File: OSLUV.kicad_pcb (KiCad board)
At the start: 4 copper layers, 110 x 85 mm, 244 parts, among them IC1 NCP12510ASN65T1G, IC2 SFH6156-3, IC3 INA210, IC4 AP63300WU-7, IC5 AP63300WU-7, IC6 STM32G071KBT6, IC7 TLV9001IDBVR, IC8 1ED44175N01BXTSA1, IC9 LP2985-33DBVR, J1 B08B-XASK-1-A_LF__SN_, J3 BM02B-SRSS-TB_LF__SN_, J4 BM02B-SRSS-TB_LF__SN_, J5 640445-2, J6 640445-2, J7 B5P-VH, Q1 STD3NK80ZT4, Q2 BC847, Q3 BSS138, Q4 BC807, Q6 BC847, T4 IMBG120R181M2HXTMA1, U1 OPA2356AIDGKR, U2 AZ431LANTR, U3 LM2901, U4 Prog

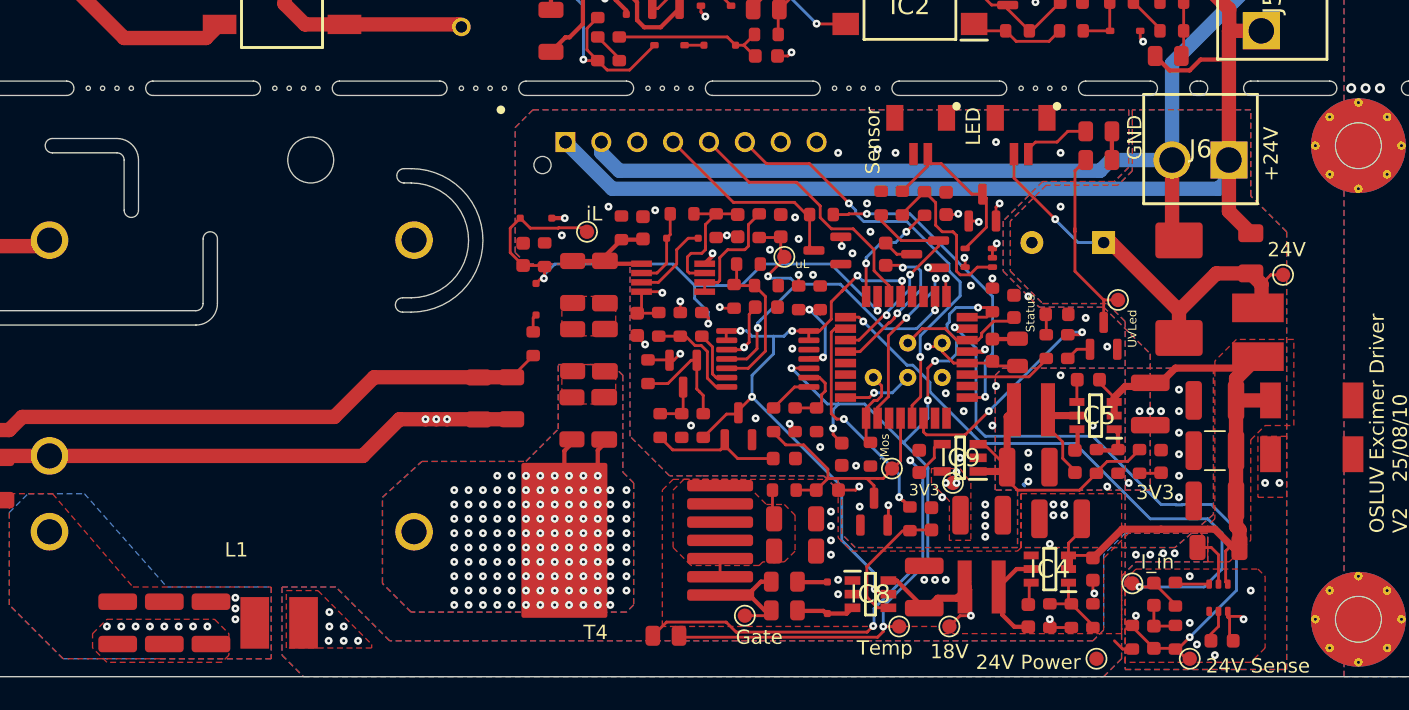
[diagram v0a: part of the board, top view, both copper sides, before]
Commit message: prototyp V2 with bug fixes
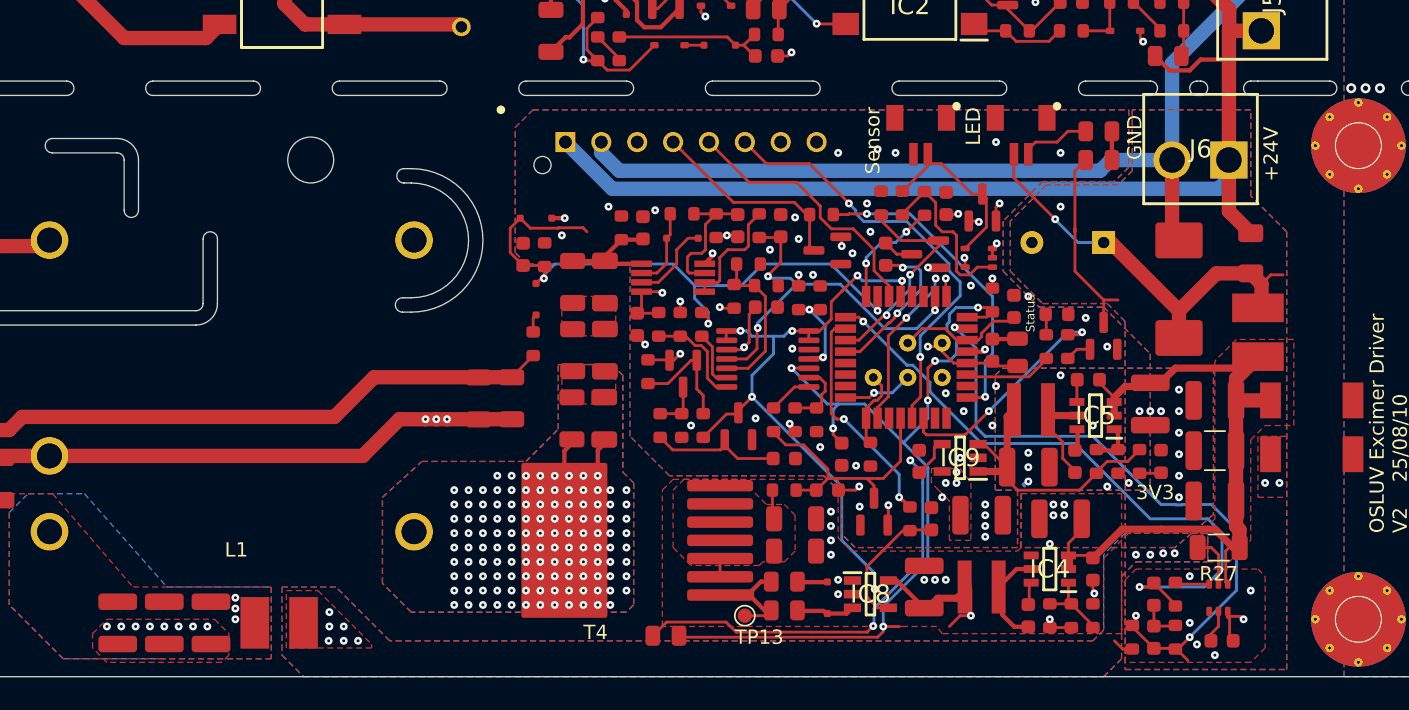
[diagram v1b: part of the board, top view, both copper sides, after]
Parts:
- removed 18V: 18V, TestPoint:TestPoint_Pad_D1.0mm
- removed 24V: 24V, TestPoint:TestPoint_Pad_D1.0mm
- removed 24V Power: VDC_Power, TestPoint:TestPoint_Pad_D1.0mm
- removed 24V Sense: 24V_Sense, TestPoint:TestPoint_Pad_D1.0mm
- removed 3V3: 3V3, TestPoint:TestPoint_Pad_D1.0mm
- removed I_in: Isense, TestPoint:TestPoint_Pad_D1.0mm
- removed REF** (x24): Loch_0,3mm, Hansmann:Loch_0,3mm
- removed Temp: Temp, TestPoint:TestPoint_Pad_D1.0mm
- removed UVLed: UV_LED, TestPoint:TestPoint_Pad_D1.0mm
- removed iL: iLamp, TestPoint:TestPoint_Pad_D1.0mm
- removed iMos: Isense_MOS, TestPoint:TestPoint_Pad_D1.0mm
- removed uL: uLamp, TestPoint:TestPoint_Pad_D1.0mm
- IC8: value 1ED44175N01BXTSA1 -> DNP; footprint Hansmann:SOT95P280X145-6N -> Hansmann_Gatetreiber:SOT95P280X145-5N
- R28: value 12k 0603 -> 10k 0603
- R46: value 3R3 0805 -> 150R 0805
- R53: value 56R 0603 -> 3k3 0603
- TP13: renamed from Gate; value Gate -> TestPoint
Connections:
- C2 pad 1: Net-(C2-Pad1) -> /excimerDriver/Isense_In
- IC8 pad 4: Net-(IC8-IN) -> +15V
- L3 pad 1: unconnected-(L3-Pad1) -> /excimerDriver/24V_FUSE
- Q3 pad 1: unconnected-(Q3-G-Pad1) -> Net-(Q3-G)
- R35 pad 2: unconnected-(R35-Pad2) -> Net-(Q3-G)
- R72 pad 1: Net-(C2-Pad1) -> /excimerDriver/Isense_In
- TP13 pad 1: Net-(T4-G) -> /excimerDriver/Isense_MOS
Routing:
- net Net-(Q3-G): track 0.00 -> 1.81 mm
- net (no net): track 1.81 -> 0.00 mm
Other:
- board text added: "DNP"

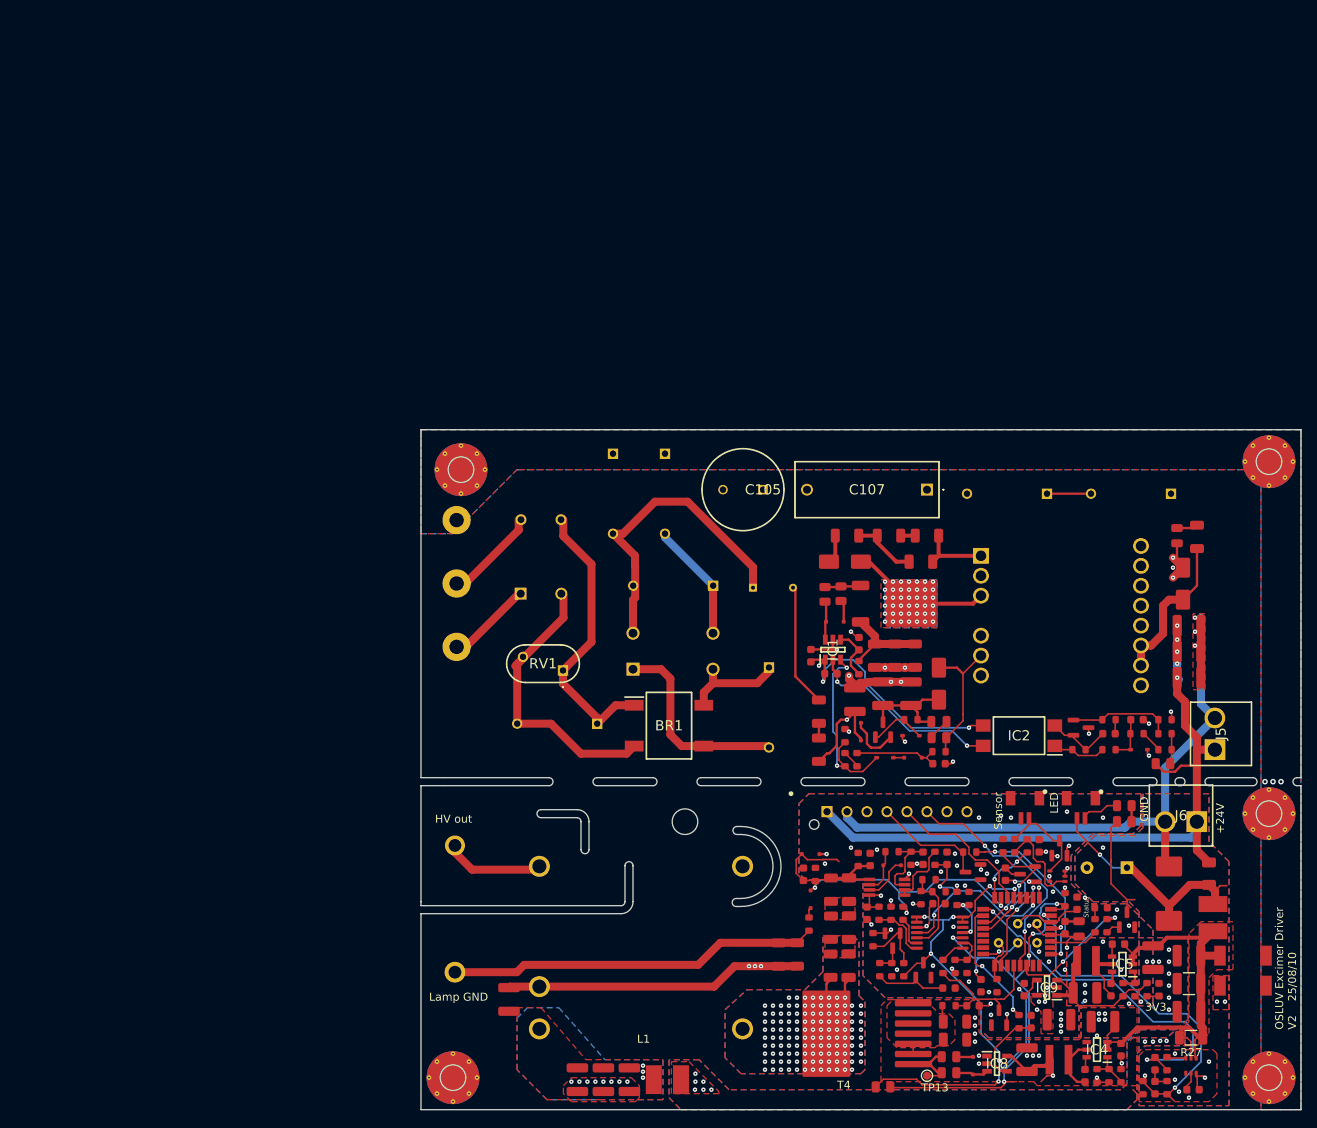
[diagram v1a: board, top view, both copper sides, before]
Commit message: prototyp V2 with fixed gate driver, test points missing
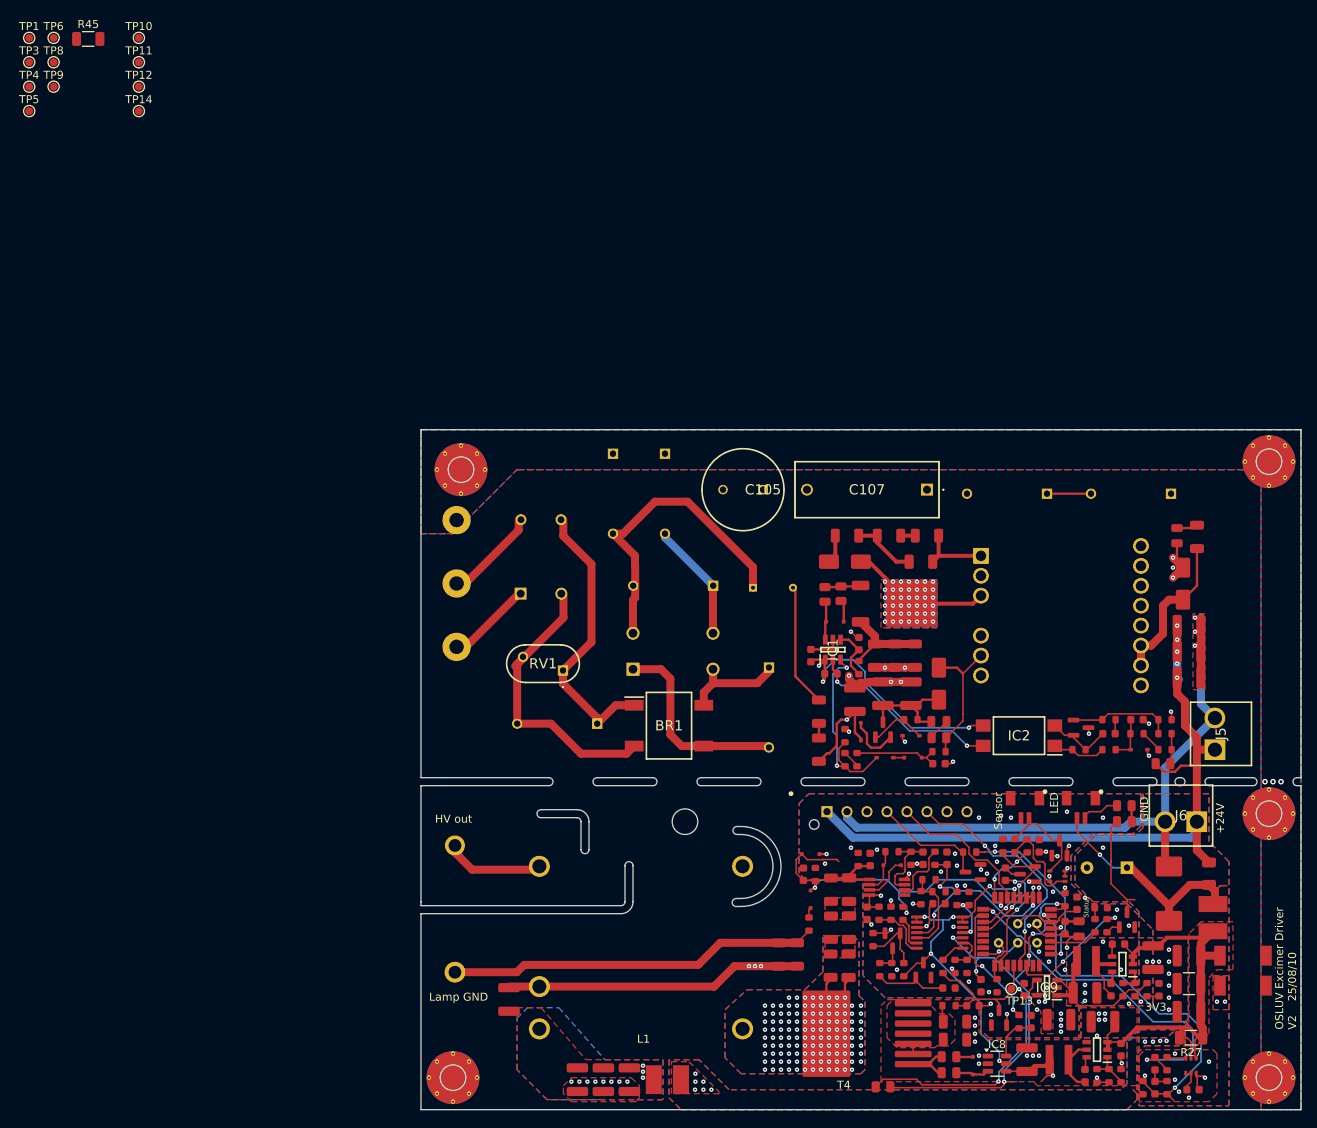
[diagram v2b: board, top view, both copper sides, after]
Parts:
- added R45: 0R02 1% 1206, Resistor_SMD:R_1206_3216Metric, F.Cu at (8.40, 1.16)
- added TP1: TestPoint, TestPoint:TestPoint_Pad_D1.0mm, F.Cu at (1.02, 1.02)
- added TP10: TestPoint, TestPoint:TestPoint_Pad_D1.0mm, F.Cu at (14.7, 1.02)
- added TP11: TestPoint, TestPoint:TestPoint_Pad_D1.0mm, F.Cu at (14.7, 4.08)
- added TP12: TestPoint, TestPoint:TestPoint_Pad_D1.0mm, F.Cu at (14.7, 7.12)
- added TP14: TestPoint, TestPoint:TestPoint_Pad_D1.0mm, F.Cu at (14.7, 10.2)
- added TP3: TestPoint, TestPoint:TestPoint_Pad_D1.0mm, F.Cu at (1.02, 4.08)
- added TP4: TestPoint, TestPoint:TestPoint_Pad_D1.0mm, F.Cu at (1.02, 7.12)
- added TP5: TestPoint, TestPoint:TestPoint_Pad_D1.0mm, F.Cu at (1.02, 10.2)
- added TP6: TestPoint, TestPoint:TestPoint_Pad_D1.0mm, F.Cu at (4.08, 1.02)
- added TP8: TestPoint, TestPoint:TestPoint_Pad_D1.0mm, F.Cu at (4.08, 4.08)
- added TP9: TestPoint, TestPoint:TestPoint_Pad_D1.0mm, F.Cu at (4.08, 7.12)
- IC8: value DNP -> 1ED44175N01BXTSA1; footprint Hansmann_Gatetreiber:SOT95P280X145-5N -> Package_TO_SOT_SMD:SOT-23-6
- TP13: value TestPoint -> iMos
- moved TP13 15.1 mm to (123.8, 119.9)
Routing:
- net Net-(IC8-IN): track 8.99 -> 5.46 mm
- net Net-(T4-G): track 5.87 -> 4.40 mm

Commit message: prototyp V2 with fixed gate driver, test points placed
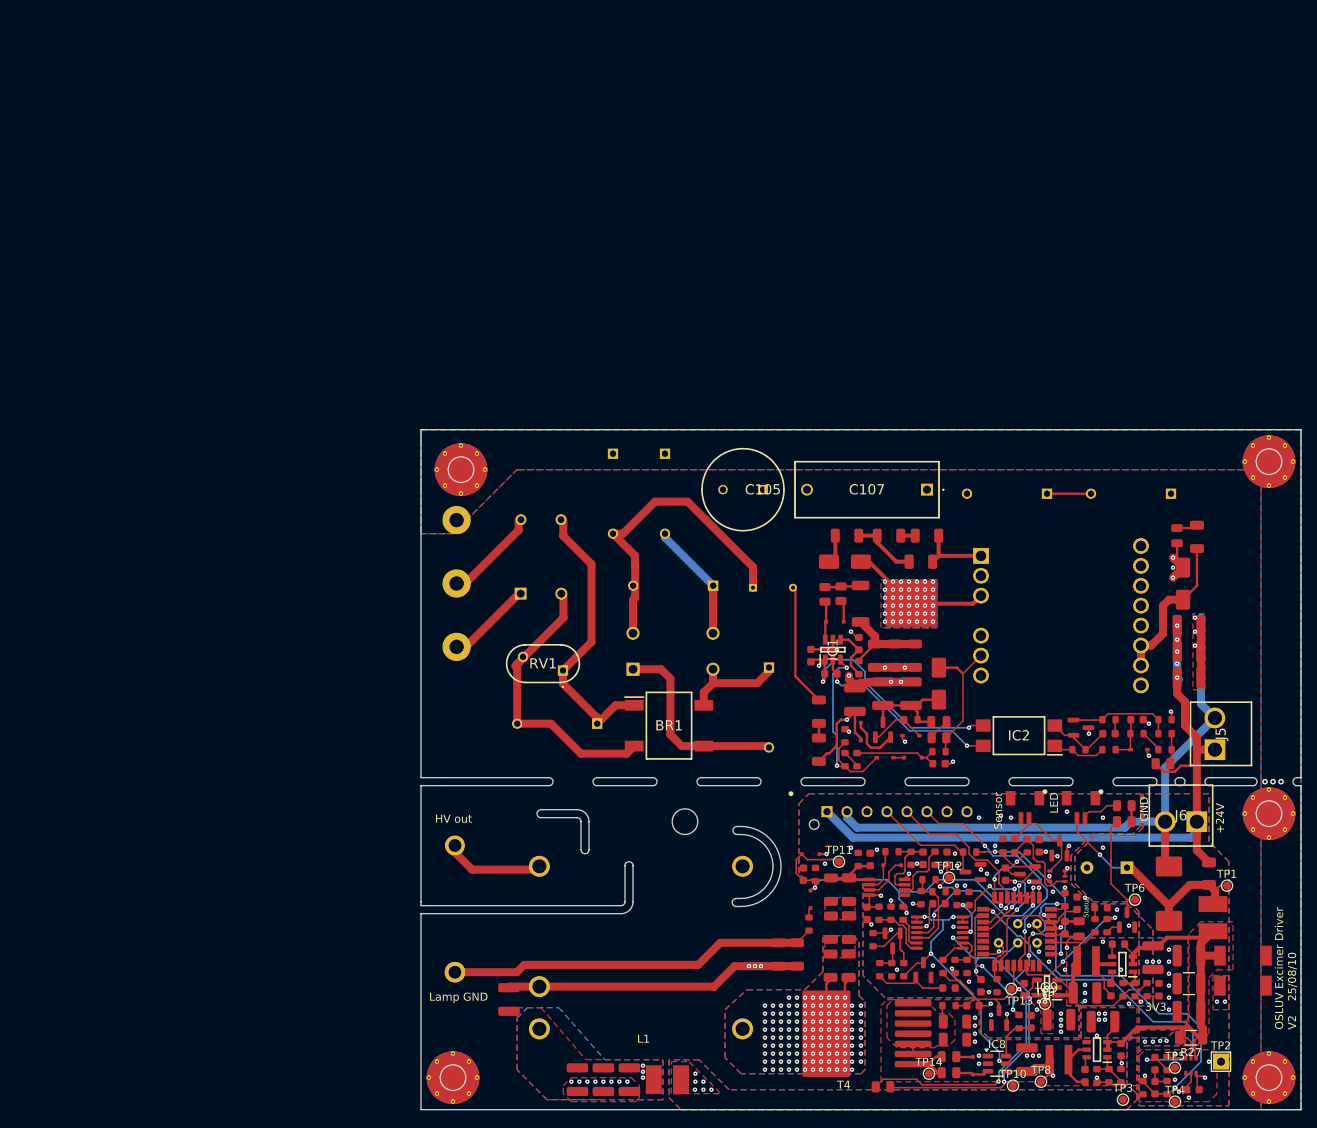
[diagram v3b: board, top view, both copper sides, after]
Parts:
- removed R45: 0R02 1% 1206, Resistor_SMD:R_1206_3216Metric
- added TP2: GND, TestPoint:TestPoint_THTPad_2.0x2.0mm_Drill1.0mm, F.Cu at (150.0, 129.0)
- TP1: value TestPoint -> 24V
- TP10: value TestPoint -> Temp
- TP11: value TestPoint -> iLamp
- TP12: value TestPoint -> uLamp
- TP13: value iMos -> iMOS
- TP14: value TestPoint -> Gate
- TP3: value TestPoint -> 24V Power
- TP4: value TestPoint -> 24V sense
- TP5: value TestPoint -> iIn
- TP6: value TestPoint -> UV LED
- TP8: value TestPoint -> 18V
- TP9: value TestPoint -> 3V3
- moved TP4 191.3 mm to (144.2, 134.0)
- moved TP3 188.4 mm to (137.8, 133.8)
- moved TP5 186.6 mm to (144.2, 129.8)
- moved TP1 183.4 mm to (150.8, 107.0)
- moved TP8 177.4 mm to (127.5, 131.5)
- moved TP6 172.8 mm to (139.2, 108.8)
- moved TP10 170.6 mm to (124.0, 132.0)
- moved TP9 168.8 mm to (128.0, 121.8)
- moved TP14 155.7 mm to (113.5, 130.5)
- moved TP12 141.5 mm to (116.0, 106.0)
- moved TP11 132.8 mm to (102.2, 104.0)
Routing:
- net Net-(T4-G): track 4.40 -> 6.04 mm
- net /excimerDriver/Isense_In: track 45.2 -> 46.3 mm

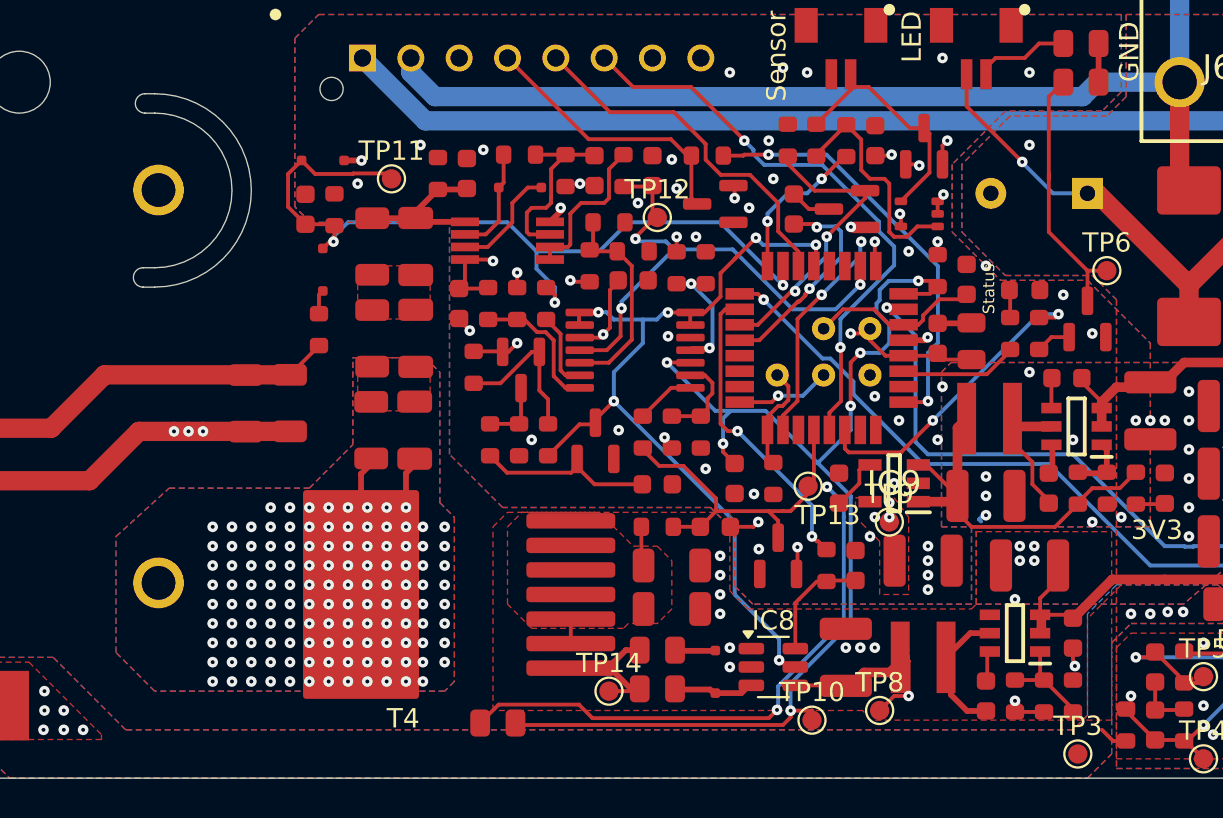
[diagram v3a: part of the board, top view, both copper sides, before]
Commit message: changed to THT MOSFET
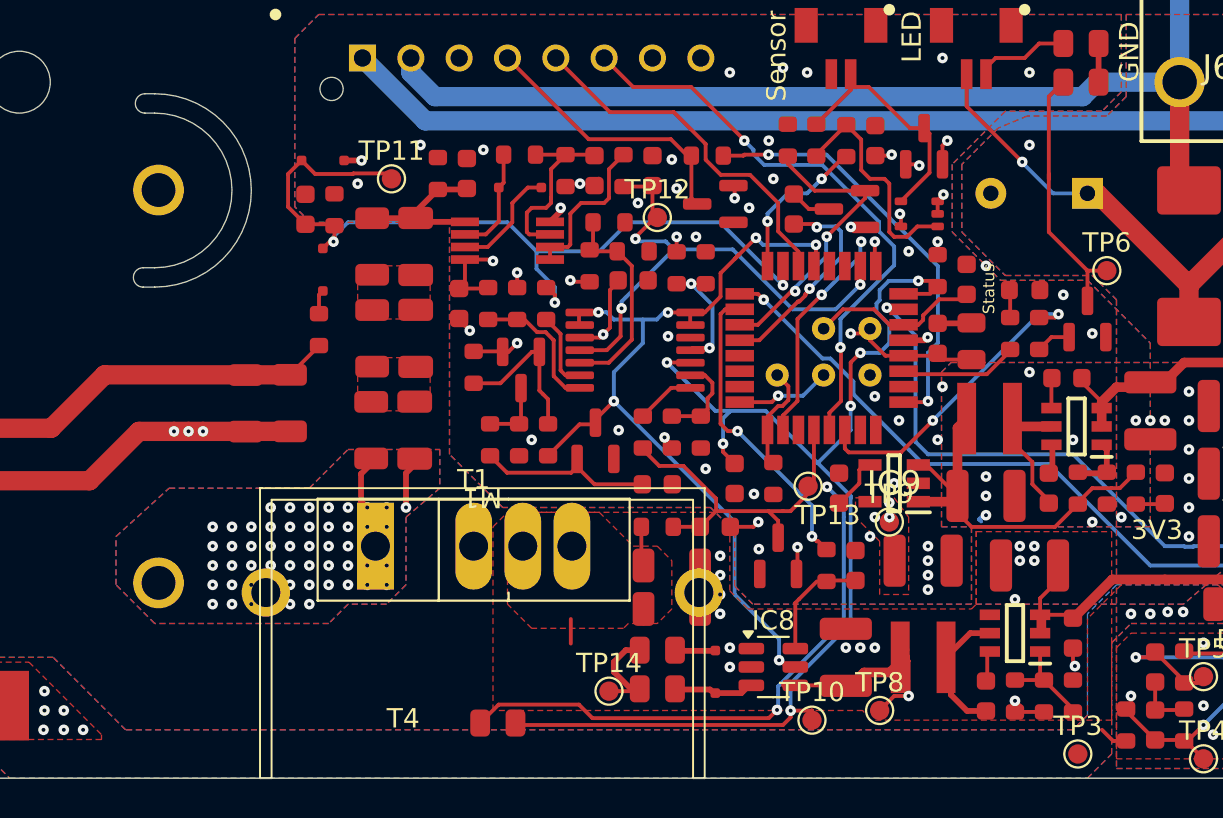
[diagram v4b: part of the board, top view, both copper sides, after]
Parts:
- removed T4: IMBG120R181M2HXTMA1, Hansmann:TO-263-7_TabPin2_HV
- added M1: ~, Hansmann_Kühlkörper:FK 274 MI 247 V, F.Cu at (107.0, 120.0)
- added T1: T_NMOS_DSKG, Package_TO_SOT_THT:TO-247-4_Vertical, F.Cu at (101.4, 123.0)
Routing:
- net Net-(T1-G): track 6.04 -> 7.31 mm
- net /excimerDriver/lampDriver/Source: track 4.03 -> 2.76 mm
- net /excimerDriver/lampDriver/HV_Drain: vias 124 -> 54
- added copper zone on F.Cu, net /excimerDriver/VDC_filter
- removed copper zone on F.Cu, net /excimerDriver/24V_FUSE
